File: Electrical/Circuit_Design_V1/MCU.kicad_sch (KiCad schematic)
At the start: 10 parts, among them U1 STM32G474RETx

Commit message: #3 Making symbols.
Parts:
- C10, C2, C3, C4, C5, C6, C7, C8, C9: footprint (none) -> Capacitor_SMD:C_0603_1608Metric
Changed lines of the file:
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@@
 			)
 		)
-		(property "Footprint" ""
+		(property "Footprint" "Capacitor_SMD:C_0603_1608Metric"
 			(at 82.55 76.5048 0)
 			(effects
@@
 			)
 		)
-		(property "Footprint" ""
+		(property "Footprint" "Capacitor_SMD:C_0603_1608Metric"
 			(at 82.55 81.5848 0)
 			(effects
@@
 			)
 		)
-		(property "Footprint" ""
+		(property "Footprint" "Capacitor_SMD:C_0603_1608Metric"
 			(at 87.3252 111.76 0)
 			(effects
@@
 			)
 		)
-		(property "Footprint" ""
+		(property "Footprint" "Capacitor_SMD:C_0603_1608Metric"
 			(at 113.03 157.1752 0)
 			(effects
@@
 			)
 		)
-		(property "Footprint" ""
+		(property "Footprint" "Capacitor_SMD:C_0603_1608Metric"
 			(at 64.77 155.2448 0)
 			(effects
@@
 			)
 		)
-		(property "Footprint" ""
+		(property "Footprint" "Capacitor_SMD:C_0603_1608Metric"
 			(at 98.0948 105.41 0)
 			(effects
@@
 			)
 		)
-		(property "Footprint" ""
+		(property "Footprint" "Capacitor_SMD:C_0603_1608Metric"
 			(at 82.55 66.3448 0)
 			(effects
@@
 			)
 		)
-		(property "Footprint" ""
+		(property "Footprint" "Capacitor_SMD:C_0603_1608Metric"
 			(at 82.55 61.2648 0)
 			(effects
@@
 			)
 		)
-		(property "Footprint" ""
+		(property "Footprint" "Capacitor_SMD:C_0603_1608Metric"
 			(at 82.55 71.4248 0)
 			(effects

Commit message: #3 Finishing some circuitry.
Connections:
- net INK_D/C#: now reaches U1.33 (PB11)
- net INK_CS#: now reaches U1.34 (PB12)
- net INK_SCL: now reaches U1.35 (PB13)
- net INK_BUSY: now reaches U1.36 (PB14)
- net INK_SDA: now reaches U1.37 (PB15)
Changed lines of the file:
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@@
+	(wire
+		(pts
+			(xy 180.34 55.88) (xy 180.34 62.23)
+		)
+		(stroke
+			(width 0)
+			(type default)
+		)
+	)
 	(wire
 		(pts
@@
 	(wire
 		(pts
+			(xy 182.88 55.88) (xy 182.88 62.23)
+		)
+		(stroke
+			(width 0)
+			(type default)
+		)
+	)
+	(wire
+		(pts
 			(xy 49.53 161.29) (xy 49.53 156.21)
 		)
@@
 	(wire
 		(pts
+			(xy 187.96 55.88) (xy 187.96 62.23)
+		)
+		(stroke
+			(width 0)
+			(type default)
+		)
+	)
+	(wire
+		(pts
 			(xy 92.71 77.47) (xy 101.6 77.47)
 		)
@@
 	(wire
 		(pts
+			(xy 185.42 55.88) (xy 185.42 62.23)
+		)
+		(stroke
+			(width 0)
+			(type default)
+		)
+	)
+	(wire
+		(pts
 			(xy 74.93 62.23) (xy 69.85 62.23)
 		)
@@
 		(pts
 			(xy 144.78 97.79) (xy 144.78 101.6)
+		)
+		(stroke
+			(width 0)
+			(type default)
+		)
+	)
+	(wire
+		(pts
+			(xy 190.5 55.88) (xy 190.5 62.23)
 		)
 		(stroke
@@
 		)
 	)
+	(global_label "INK_SCL"
+		(shape input)
+		(at 185.42 55.88 90)
+		(fields_autoplaced yes)
+		(effects
+			(font
+				(size 1.27 1.27)
+			)
+			(justify left)
+		)
+		(property "Intersheetrefs" "${INTERSHEET_REFS}"
+			(at 185.42 45.2143 90)
+			(effects
+				(font
+					(size 1.27 1.27)
+				)
+				(justify left)
+				(hide yes)
+			)
+		)
+	)
 	(global_label "ADX_SCLK"
 		(shape input)
@@
 		)
 	)
+	(global_label "INK_SDA"
+		(shape input)
+		(at 190.5 55.88 90)
+		(fields_autoplaced yes)
+		(effects
+			(font
+				(size 1.27 1.27)
+			)
+			(justify left)
+		)
+		(property "Intersheetrefs" "${INTERSHEET_REFS}"
+			(at 190.5 45.1538 90)
+			(effects
+				(font
+					(size 1.27 1.27)
+				)
+				(justify left)
+				(hide yes)
+			)
+		)
+	)
+	(global_label "INK_D{slash}C#"
+		(shape input)
+		(at 180.34 55.88 90)
+		(fields_autoplaced yes)
+		(effects
+			(font
+				(size 1.27 1.27)
+			)
+			(justify left)
+		)
+		(property "Intersheetrefs" "${INTERSHEET_REFS}"
+			(at 180.34 43.5814 90)
+			(effects
+				(font
+					(size 1.27 1.27)
+				)
+				(justify left)
+				(hide yes)
+			)
+		)
+	)
 	(global_label "ADX_INT1"
 		(shape output)
@@
 		)
 	)
+	(global_label "INK_CS#"
+		(shape input)
+		(at 182.88 55.88 90)
+		(fields_autoplaced yes)
+		(effects
+			(font
+				(size 1.27 1.27)
+			)
+			(justify left)
+		)
+		(property "Intersheetrefs" "${INTERSHEET_REFS}"
+			(at 182.88 44.9724 90)
+			(effects
+				(font
+					(size 1.27 1.27)
+				)
+				(justify left)
+				(hide yes)
+			)
+		)
+	)
 	(global_label "ADX_SDI"
 		(shape input)
@@
 			(effects
 				(font
+					(size 1.27 1.27)
+				)
+				(justify left)
+				(hide yes)
+			)
+		)
+	)
+	(global_label "INK_BUSY"
+		(shape output)
+		(at 187.96 55.88 90)
+		(fields_autoplaced yes)
+		(effects
+			(font
+				(size 1.27 1.27)
+			)
+			(justify left)
+		)
+		(property "Intersheetrefs" "${INTERSHEET_REFS}"
+			(at 187.96 43.8233 90)
+			(effects
+				(font

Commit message: Finishing schematic
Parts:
- added R6, R7: 10K, Resistor_SMD:R_0805_2012Metric, symbol Device:R
- added SW1, SW2: SW_Push, Button_Switch_THT:SW_PUSH_6mm, symbol Switch:SW_Push
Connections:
- net +3V3: now also R6.2, R7.1
- net GND: now also SW1.1, SW2.1
- net at U1.3 (PC14): now also R7.2, SW2.2
- net at U1.4 (PC15): now also R6.1, SW1.2

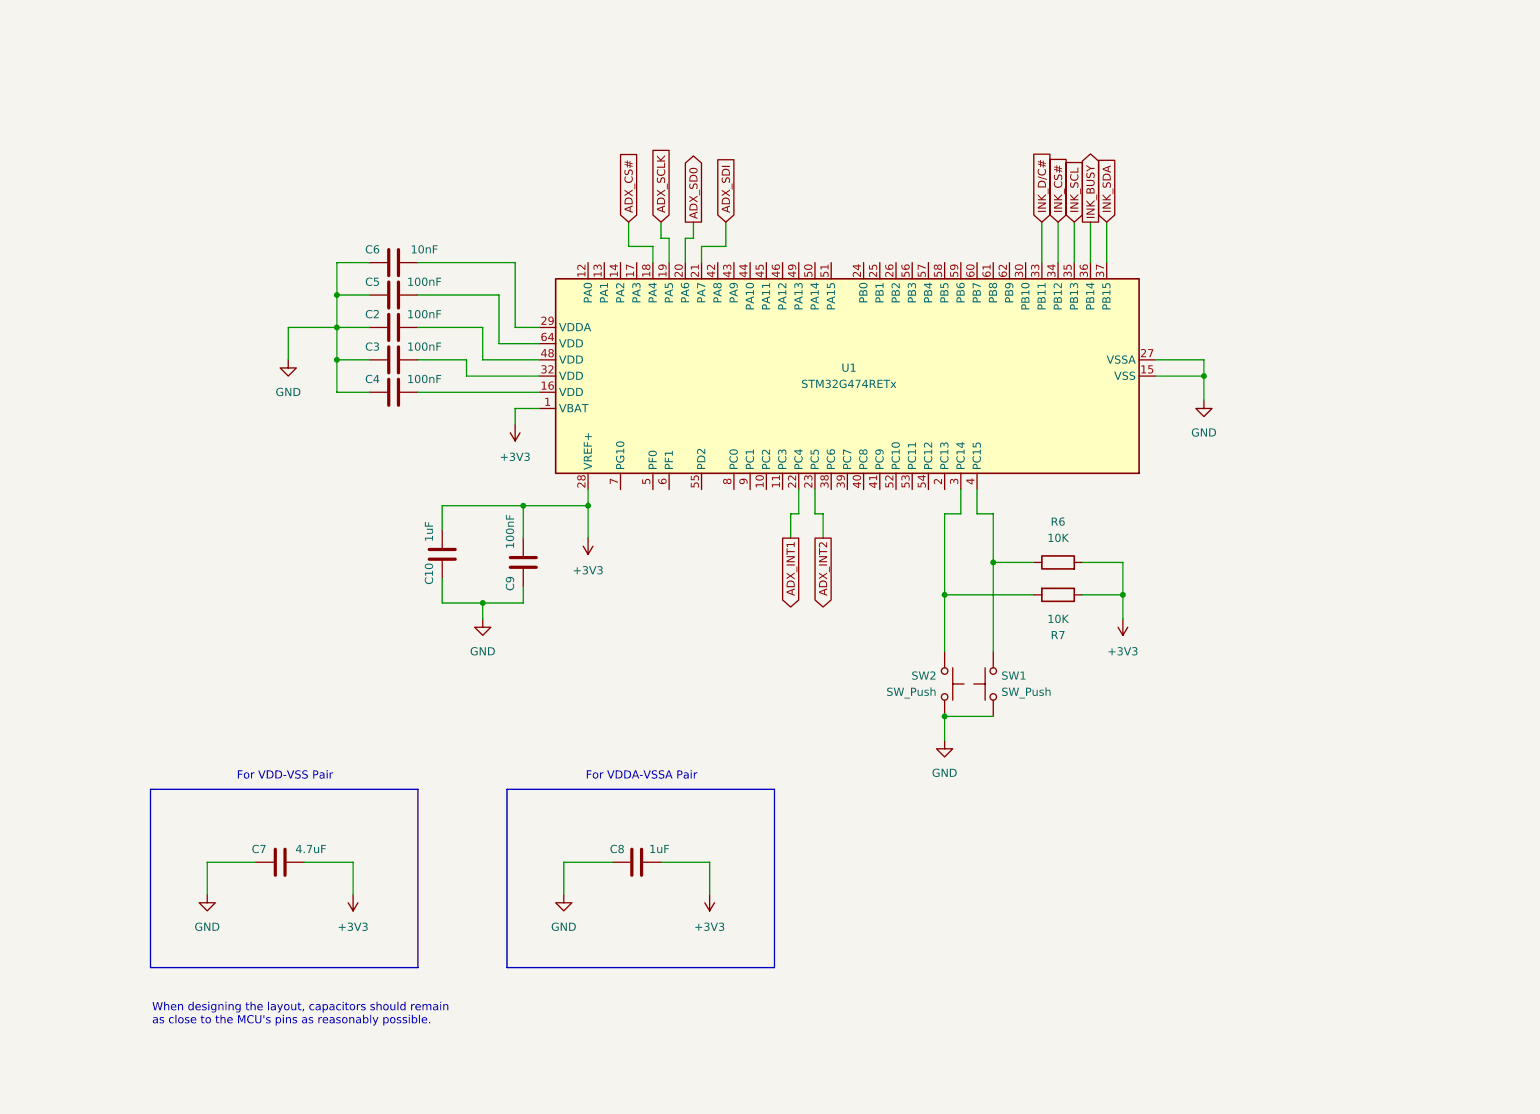
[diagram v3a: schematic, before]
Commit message: Completing schematic.
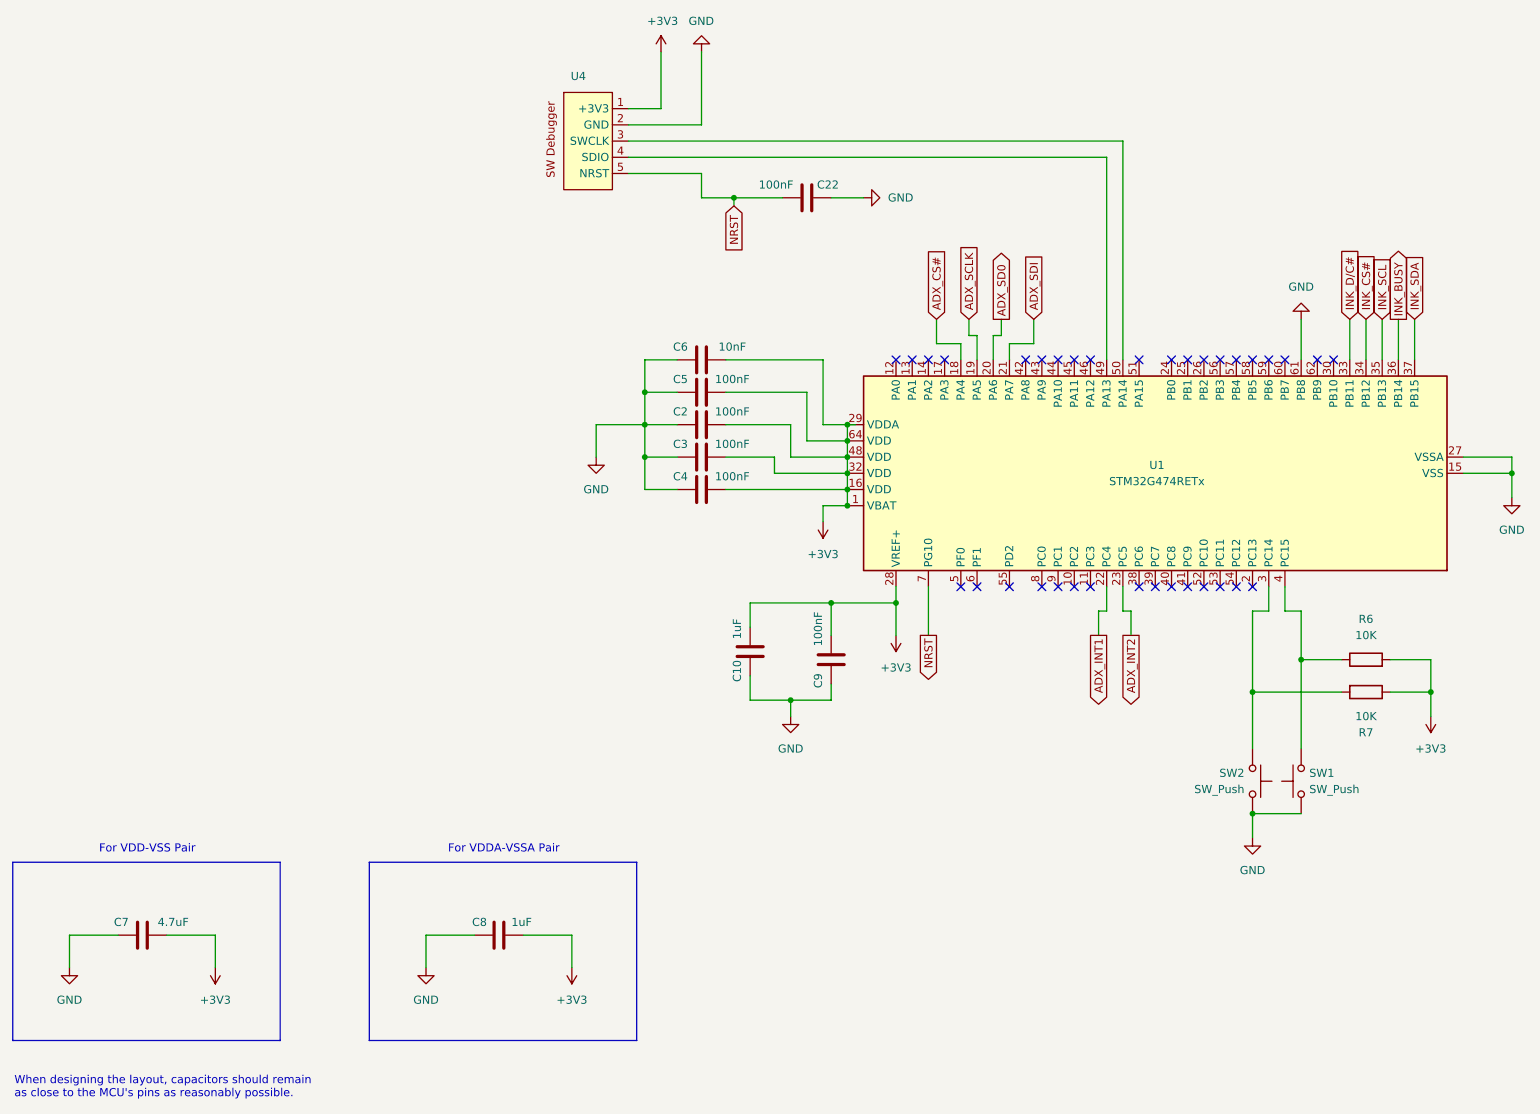
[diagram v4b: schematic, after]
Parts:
- added C22: 100nF, Capacitor_SMD:C_0603_1608Metric, symbol Device:C
- added U4: ~, Etchasketch_Footprints:SW Pin Headers, symbol Etchasketch_hardware_symbol_library:SW_Debugger_and_Programmer
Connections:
- net +3V3: now also C2.2, C3.2, C4.2, C5.2, C6.2, U1.16 (VDD), U1.29 (VDDA), U1.32 (VDD), U1.48 (VDD), U1.64 (VDD), U4.1 (+3V3)
- net GND: now also U1.61 (PB8), C22.1, U4.2 (GND)
- net at U1.49 (PA13): now also U4.4 (SDIO)
- net at U1.50 (PA14): now also U4.3 (SWCLK)
- net NRST: now reaches U1.7 (PG10)
- net NRST: now also C22.2, U4.5 (NRST)
- no-connect marks 0 -> 35
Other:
- moved on the sheet: C10, C2, C3, C4, C5, C6, C7, C8, C9, R6, R7, SW1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

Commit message: Adding pots.
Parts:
- added RV1: R_Potentiometer, Etchasketch_Footprints:Potentiometer, symbol Device:R_Potentiometer
- added RV2: 10k, Etchasketch_Footprints:Potentiometer, symbol Device:R_Potentiometer
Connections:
- net +3V3: now also RV1.2, RV2.2
- net GND: now also RV1.3, RV2.3
- net at U1.59 (PB6): now also RV2.1
- net at U1.60 (PB7): now also RV1.1
- no-connect marks 35 -> 33
